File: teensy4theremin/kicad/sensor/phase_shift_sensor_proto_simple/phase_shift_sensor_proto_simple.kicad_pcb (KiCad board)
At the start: 2 copper layers, 94 x 35.6 mm, 25 parts, among them J1 INDUCTOR_IN, J2 INDUCTOR_OUT, J3 ANTENNA, J4 SENSOR, U1 74HC04, U2 sp721, U3 REG_3V3

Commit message: update:
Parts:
- moved C6 2.54 mm to (88.9, 101.6)
- moved C3 2.54 mm to (114.3, 101.6)
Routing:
- net +3V3: track 134.7 -> 129.5 mm
- net GND: track 168.2 -> 170.7 mm
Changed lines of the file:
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@@
     (thickness 1.6)
     (drawings 18)
-    (tracks 100)
+    (tracks 99)
     (zones 0)
     (modules 25)
@@
   )
   (module Capacitor_THT:C_Disc_D4.3mm_W1.9mm_P5.00mm (layer F.Cu)
-    (at 111.76 101.6 270)
+    (at 114.3 101.6 270)
     (descr "C, Disc series, Radial, pin pitch=5.00mm, , diameter*width=4.3*1.9mm^2, Capacitor, http://www.vishay.com/docs/45233/krseries.pdf")
     (tags "C Disc series Radial pin pitch 5.00mm  diameter 4.3mm width 1.9mm Capacitor")
-    (fp_text reference C3 (at 2.54 1.905 270) (layer F.SilkS)
-      (effects (font (size 1 1) (thickness 0.15)))
-    )
-    (fp_text value 0.1uF (at 2.54 -1.905 270) (layer F.SilkS)
+    (fp_text reference C3 (at 6.985 0) (layer F.SilkS)
+      (effects (font (size 1 1) (thickness 0.15)))
+    )
+    (fp_text value 0.1uF (at 2.54 1.905 270) (layer F.SilkS)
       (effects (font (size 1 1) (thickness 0.15)))
     )
@@
   )
   (module Capacitor_THT:C_Disc_D4.3mm_W1.9mm_P5.00mm (layer F.Cu)
-    (at 86.36 101.6 270)
+    (at 88.9 101.6 270)
     (descr "C, Disc series, Radial, pin pitch=5.00mm, , diameter*width=4.3*1.9mm^2, Capacitor, http://www.vishay.com/docs/45233/krseries.pdf")
     (tags "C Disc series Radial pin pitch 5.00mm  diameter 4.3mm width 1.9mm Capacitor")
@@
     (arrow2b (pts (xy 165.1 88.9) (xy 165.686421 90.026504)))
   )
-  (segment (start 111.76 101.6) (end 111.76 99.06) (width 0.4) (layer B.Cu) (net 1))
-  (segment (start 114.3 99.06) (end 116.84 99.06) (width 0.4) (layer B.Cu) (net 1))
-  (segment (start 111.76 99.06) (end 114.3 99.06) (width 0.4) (layer B.Cu) (net 1))
   (segment (start 81.2 101.6) (end 81.28 101.52) (width 0.4) (layer B.Cu) (net 1))
   (segment (start 76.2 101.6) (end 81.2 101.6) (width 0.4) (layer B.Cu) (net 1))
-  (segment (start 86.28 101.52) (end 86.36 101.6) (width 0.4) (layer B.Cu) (net 1))
-  (segment (start 81.28 101.52) (end 86.28 101.52) (width 0.4) (layer B.Cu) (net 1))
-  (segment (start 86.36 101.6) (end 86.36 99.06) (width 0.4) (layer B.Cu) (net 1))
-  (segment (start 86.36 99.06) (end 91.44 99.06) (width 0.4) (layer B.Cu) (net 1))
+  (segment (start 88.9 101.6) (end 88.9 99.06) (width 0.4) (layer B.Cu) (net 1))
   (segment (start 91.44 99.06) (end 93.98 99.06) (width 0.4) (layer B.Cu) (net 1))
   (segment (start 93.98 96.52) (end 99.06 96.52) (width 0.4) (layer B.Cu) (net 1))
@@
   (segment (start 129.54 88.9) (end 129.54 101.6) (width 0.4) (layer B.Cu) (net 1))
   (segment (start 88.9 88.9) (end 129.54 88.9) (width 0.4) (layer B.Cu) (net 1))
-  (segment (start 86.36 99.06) (end 88.9 99.06) (width 0.4) (layer B.Cu) (net 1))
   (segment (start 88.9 99.06) (end 88.9 88.9) (width 0.4) (layer B.Cu) (net 1))
+  (segment (start 88.82 101.52) (end 88.9 101.6) (width 0.4) (layer B.Cu) (net 1))
+  (segment (start 88.9 99.06) (end 91.44 99.06) (width 0.4) (layer B.Cu) (net 1))
+  (segment (start 83.82 99.06) (end 83.82 101.52) (width 0.4) (layer B.Cu) (net 1))
+  (segment (start 81.28 101.52) (end 83.82 101.52) (width 0.4) (layer B.Cu) (net 1))
+  (segment (start 83.82 101.52) (end 88.82 101.52) (width 0.4) (layer B.Cu) (net 1))
+  (segment (start 114.3 101.6) (end 116.84 101.6) (width 0.4) (layer B.Cu) (net 1))
   (segment (start 81.12 106.36) (end 81.28 106.52) (width 0.4) (layer B.Cu) (net 2))
   (segment (start 81.12 106.68) (end 81.28 106.52) (width 0.4) (layer B.Cu) (net 2))
@@
   (segment (start 72.41137 109.22) (end 76.2 109.22) (width 0.4) (layer B.Cu) (net 2))
   (segment (start 76.2 109.22) (end 76.2 106.68) (width 0.4) (layer B.Cu) (net 2))
-  (segment (start 106.68 106.68) (end 111.76 106.68) (width 0.4) (layer B.Cu) (net 2))
   (segment (start 124.46 106.68) (end 124.46 109.22) (width 0.4) (layer B.Cu) (net 2))
-  (segment (start 111.76 109.22) (end 111.76 106.6) (width 0.4) (layer B.Cu) (net 2))
   (segment (start 101.6 119.38) (end 86.36 119.38) (width 0.4) (layer B.Cu) (net 2))
   (segment (start 124.46 109.22) (end 119.38 109.22) (width 0.4) (layer B.Cu) (net 2))
@@
   (segment (start 106.68 104.14) (end 86.36 104.14) (width 0.25) (layer F.Cu) (net 2))
   (segment (start 86.36 104.14) (end 86.36 106.6) (width 0.25) (layer F.Cu) (net 2))
+  (segment (start 114.22 106.68) (end 114.3 106.6) (width 0.4) (layer B.Cu) (net 2))
+  (segment (start 106.68 106.68) (end 114.22 106.68) (width 0.4) (layer B.Cu) (net 2))
+  (segment (start 114.3 109.22) (end 114.3 106.68) (width 0.4) (layer B.Cu) (net 2))
   (segment (start 96.52 116.84) (end 96.52 106.68) (width 0.4) (layer B.Cu) (net 5))
   (segment (start 71.2 104.14) (end 71.12 104.06) (width 0.4) (layer B.Cu) (net 7))
@@
   (segment (start 134.62 106.68) (end 132.08 106.68) (width 0.4) (layer B.Cu) (net 17))
   (segment (start 132.08 106.68) (end 129.54 106.68) (width 0.4) (layer B.Cu) (net 17))
-  (segment (start 139.7 96.6) (end 142.24 96.6) (width 0.4) (layer B.Cu) (net 18))
-  (segment (start 139.62 96.52) (end 139.7 96.6) (width 0.4) (layer B.Cu) (net 18))
   (segment (start 137.16 104.14) (end 137.16 96.52) (width 0.4) (layer B.Cu) (net 18))
   (segment (start 134.62 96.52) (end 137.16 96.52) (width 0.4) (layer B.Cu) (net 18))
-  (segment (start 137.16 96.52) (end 139.62 96.52) (width 0.4) (layer B.Cu) (net 18))
+  (segment (start 142.16 96.52) (end 142.24 96.6) (width 0.4) (layer B.Cu) (net 18))
+  (segment (start 137.16 96.52) (end 142.16 96.52) (width 0.4) (layer B.Cu) (net 18))
   (segment (start 104.14 111.76) (end 104.14 106.68) (width 0.4) (layer B.Cu) (net 19))
   (segment (start 99.06 116.84) (end 99.06 111.76) (width 0.4) (layer B.Cu) (net 19))

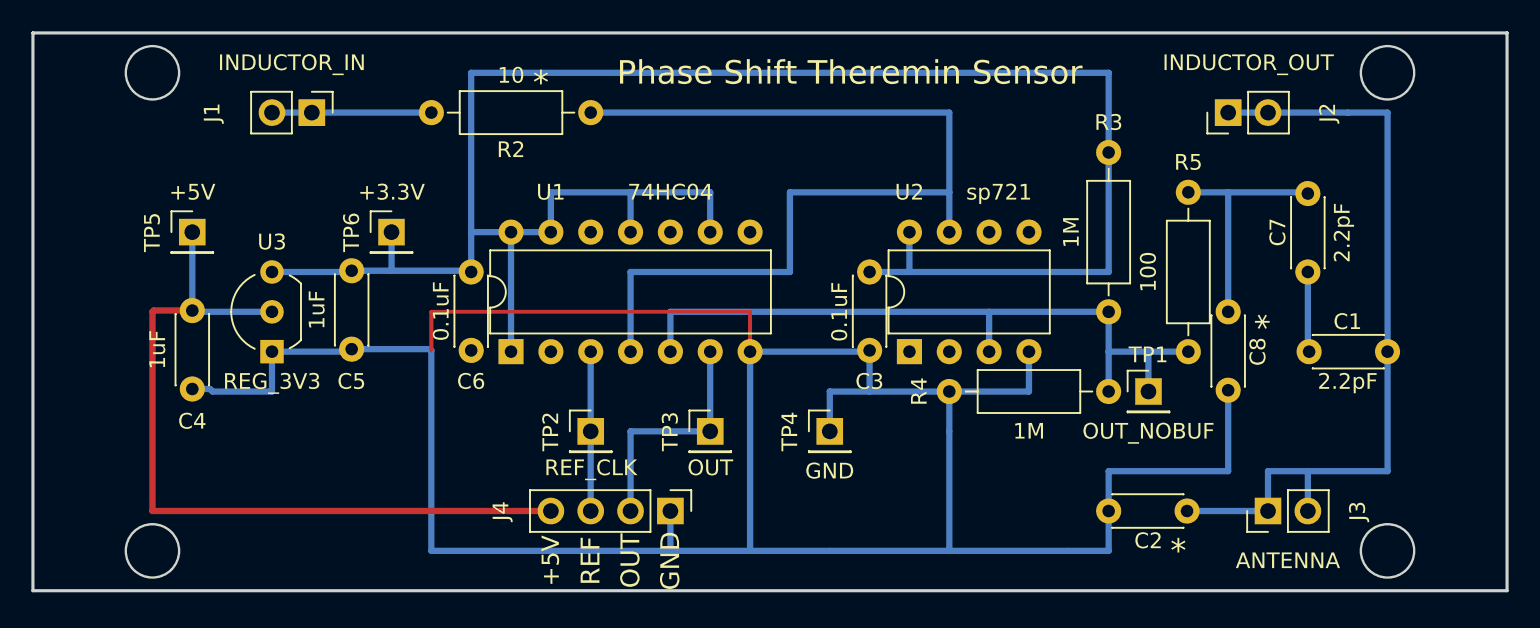
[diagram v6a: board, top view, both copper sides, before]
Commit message: update prototype phase sensor board
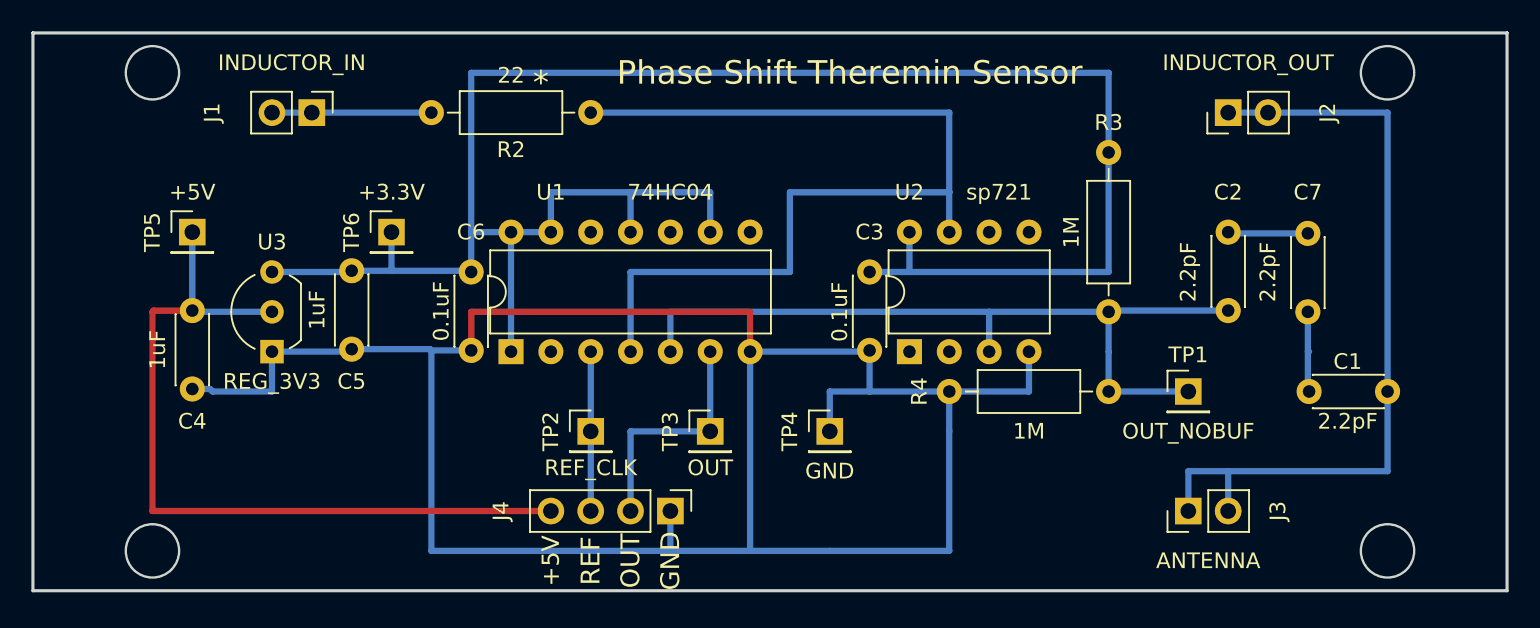
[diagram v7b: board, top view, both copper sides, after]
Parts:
- removed C8: 6.8pF, Capacitor_THT:C_Disc_D4.3mm_W1.9mm_P5.00mm
- removed R5: 100, Resistor_THT:R_Axial_DIN0207_L6.3mm_D2.5mm_P10.16mm_Horizontal
- C2: value 0.1pF -> 2.2pF
- R2: value 10 -> 22
- moved C2 19.3 mm to (137.2, 99.1), turned to 270 degrees
- moved J3 5.08 mm to (134.6, 116.8)
- moved C7 2.54 mm to (142.2, 104.1)
- moved C1 2.54 mm to (147.3, 109.2)
- moved TP1 2.54 mm to (134.6, 109.2)
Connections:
- C2 pad 1: GND -> Net-(C2-Pad1)
- C2 pad 2: Net-(C1-Pad1) -> Net-(C2-Pad2)
- C7 pad 2: Net-(C7-Pad2) -> Net-(C2-Pad1)
- R3 pad 2: Net-(R3-Pad2) -> Net-(C2-Pad2)
- R4 pad 1: Net-(R3-Pad2) -> Net-(C2-Pad2)
- TP1 pad 1: Net-(R3-Pad2) -> Net-(C2-Pad2)
- U1 pad 5: Net-(R3-Pad2) -> Net-(C2-Pad2)
- U2 pad 3: Net-(R3-Pad2) -> Net-(C2-Pad2)
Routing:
- net Net-(C2-Pad2): track 0.00 -> 50.8 mm
- net Net-(R3-Pad2): track 45.7 -> 0.00 mm
- net GND: track 170.7 -> 142.7 mm
- net Net-(C7-Pad2): track 15.3 -> 0.00 mm
- net Net-(C2-Pad1): track 0.00 -> 5.23 mm
